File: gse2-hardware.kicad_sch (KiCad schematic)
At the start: 83 parts, among them J1 PJ-002A, J2 PJ-002A, J3 ARM Cortex Debug, J4 USB-C, J47 DSUB_15pin/VGA Veritical Fema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, J6 ARM, J7 0430451812, Q1 DMG3402L, U1 STM32F105RCT6, U2 AS78L05RTR-E1, U3 USBLC6-2SC6, U5 MP2338GTL-Z, U6 UA78M10CKVURG3, U7 BA78M20FP-E2, U8 MAX11614, Y1 16MHz

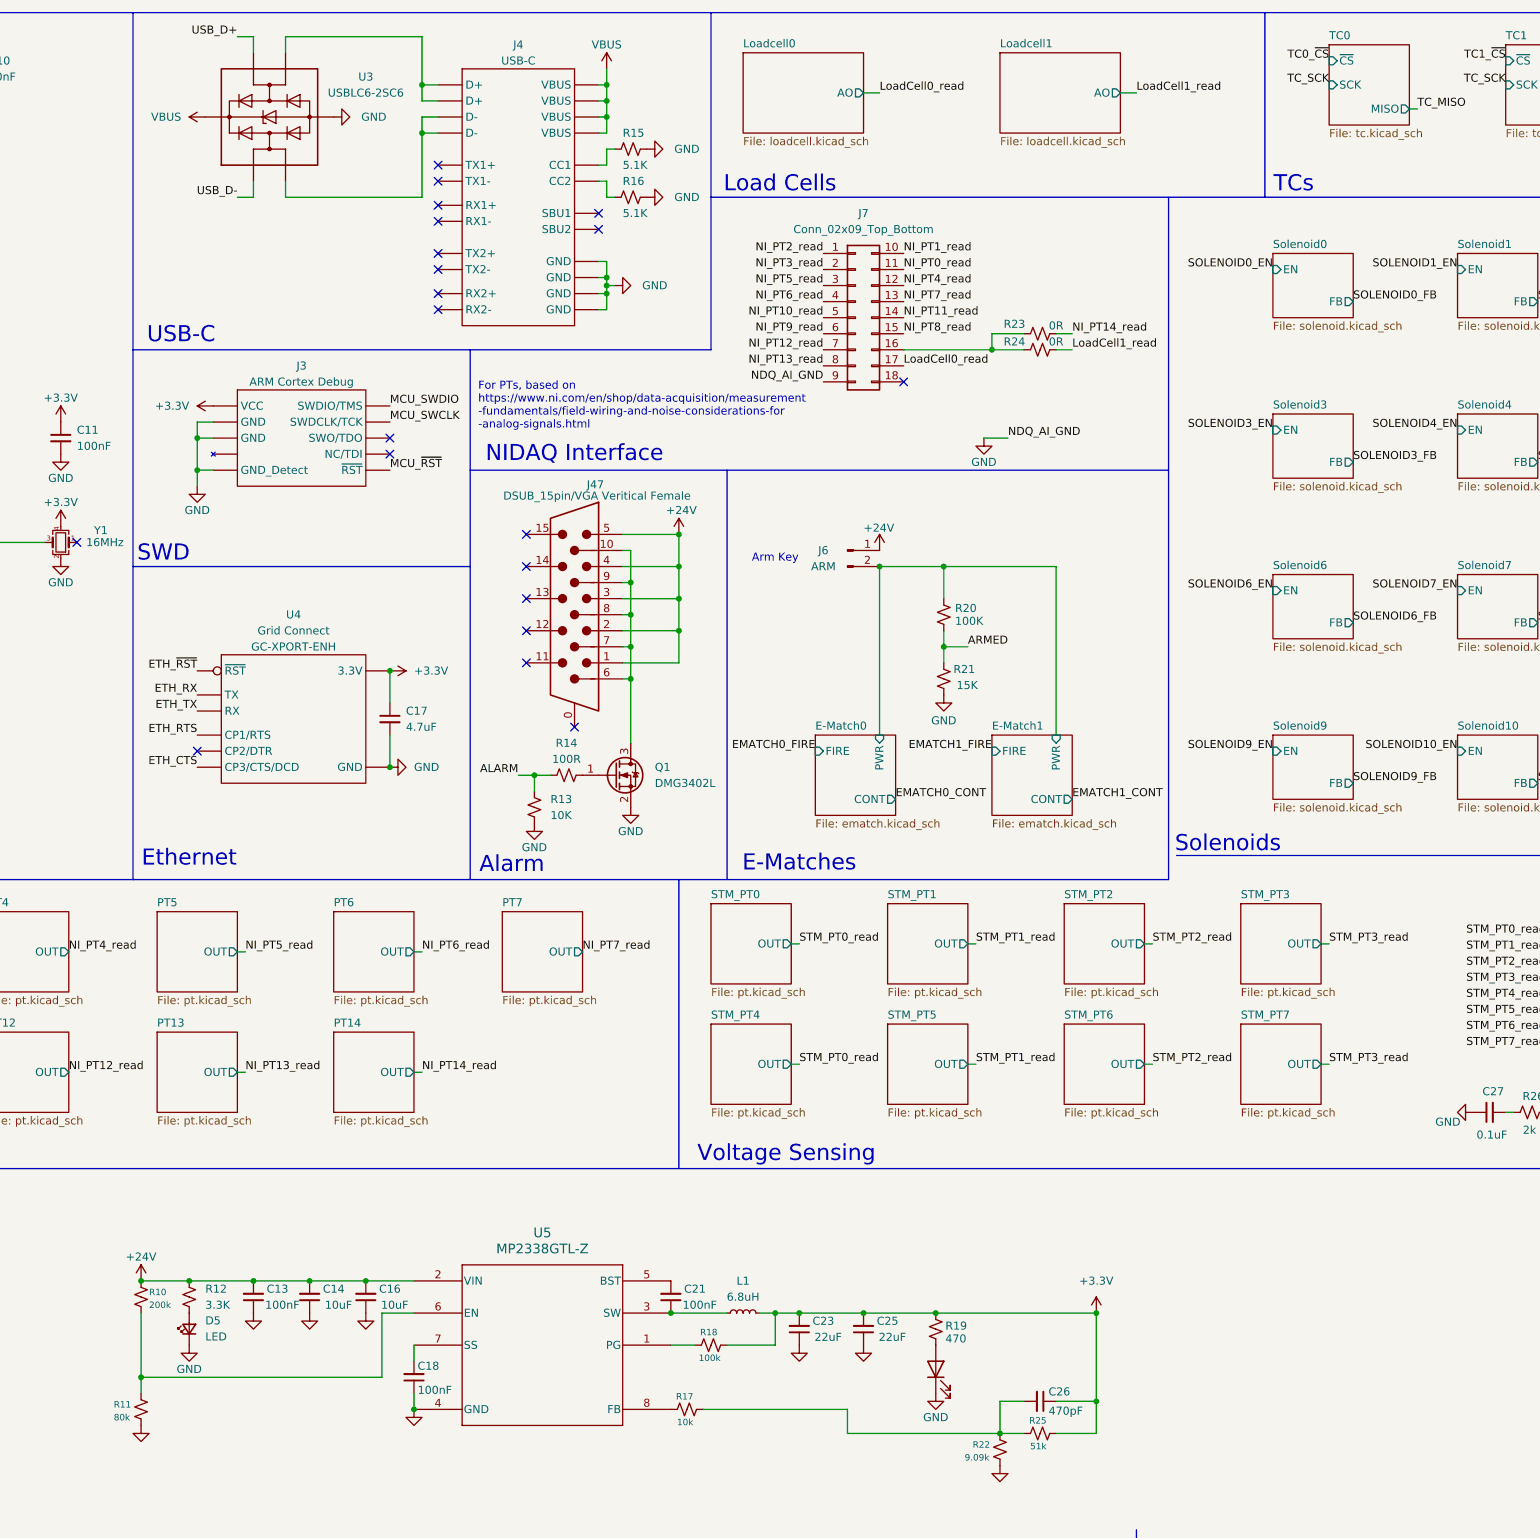
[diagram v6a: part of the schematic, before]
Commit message: GSE v2.1: Routing 90% done
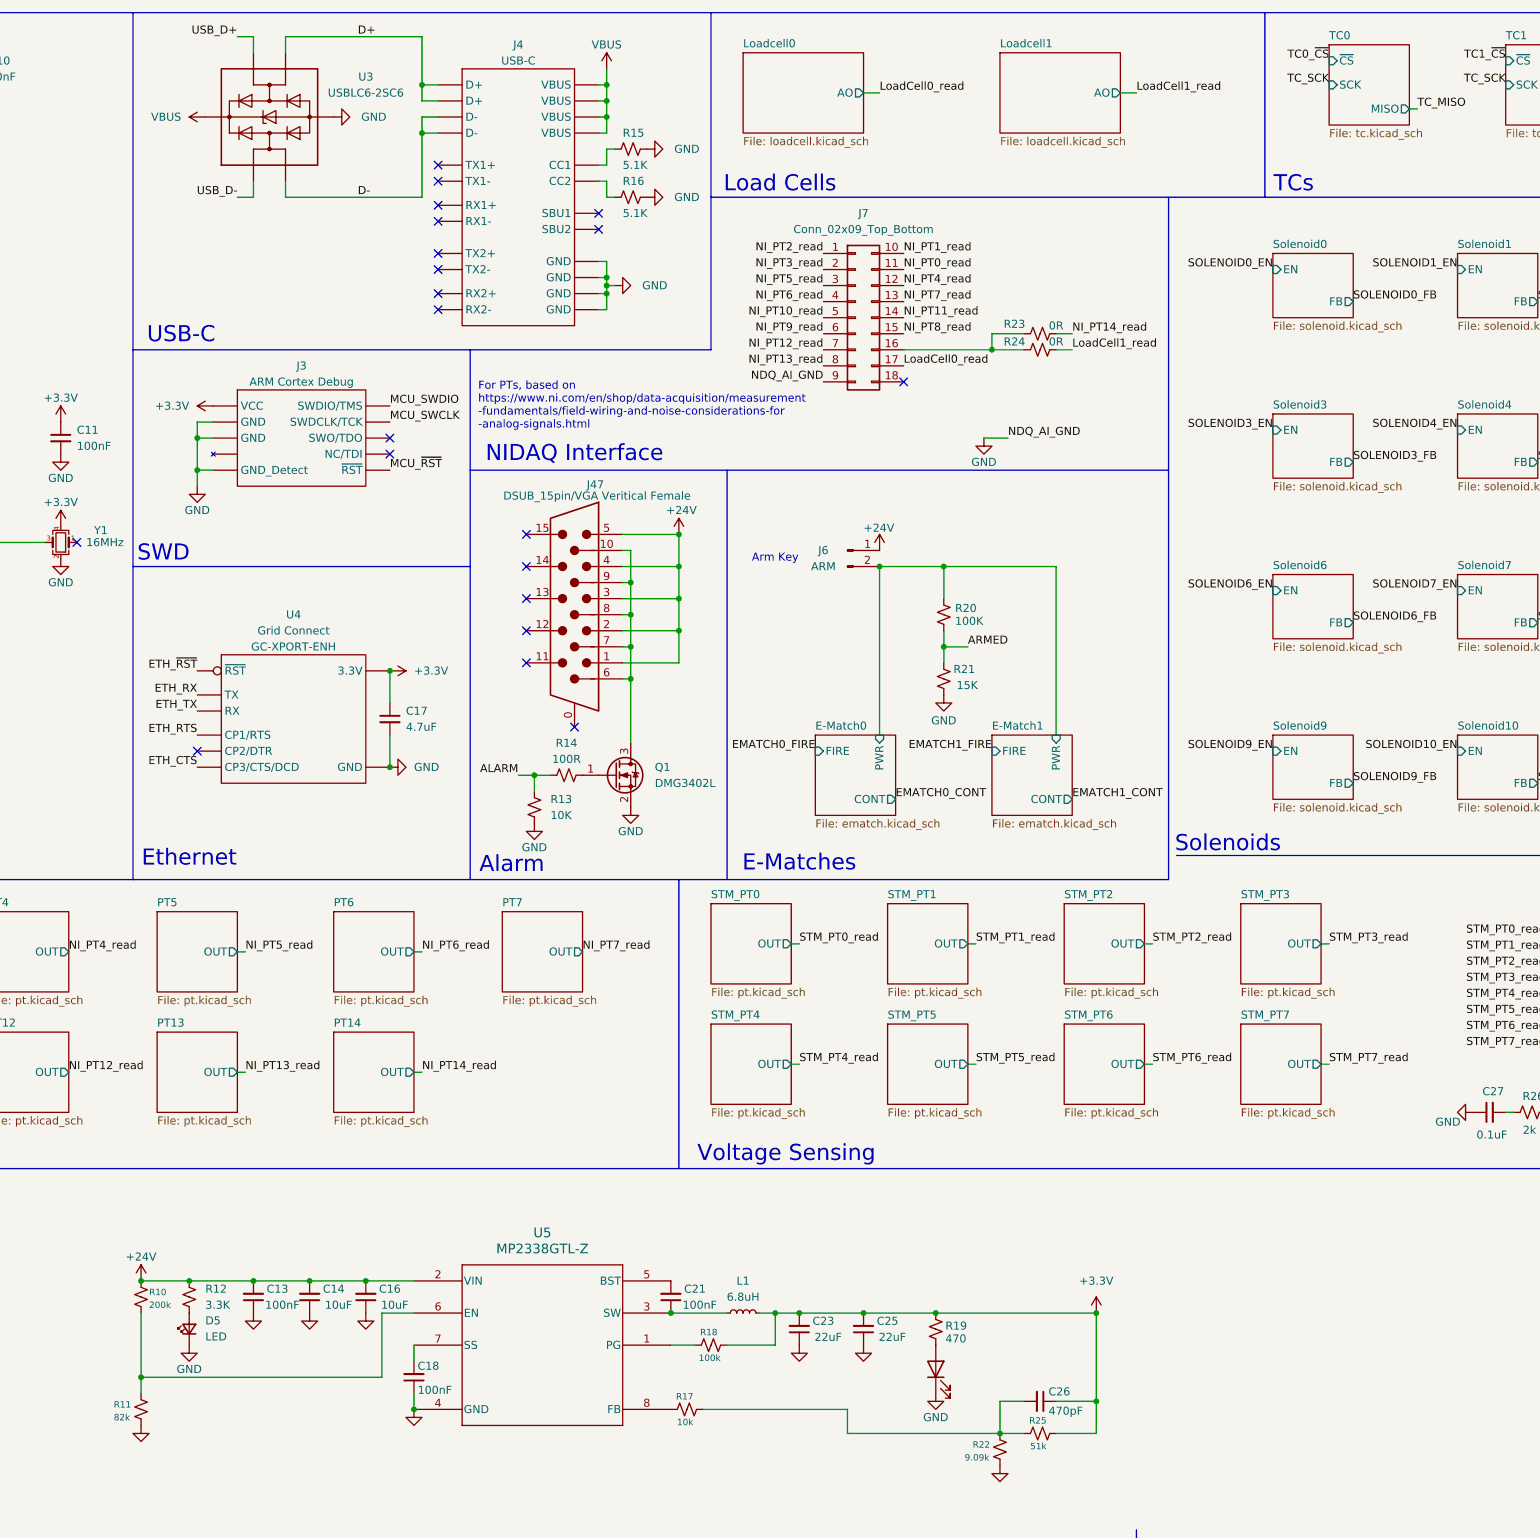
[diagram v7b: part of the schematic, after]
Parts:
- R11: value 80k -> 82k
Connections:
- net D-: now reaches J4.A7 (D-), J4.B7 (D-), U3.1 (I/O1)
- net D+: now reaches J4.A6 (D+), J4.B6 (D+), U3.3 (I/O2)
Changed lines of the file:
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@@
 		)
 	)
-	(label "STM_PT2_read"
-		(at 302.26 179.07 0)
-		(effects
-			(font
-				(size 1.27 1.27)
-			)
-			(justify left bottom)
-		)
-	)
 	(label "TC_SCK"
 		(at 55.88 121.92 180)
@@
 		)
 	)
+	(label "STM_PT5_read"
+		(at 274.32 179.07 0)
+		(effects
+			(font
+				(size 1.27 1.27)
+			)
+			(justify left bottom)
+		)
+	)
 	(label "NI_PT9_read"
 		(at 52.07 180.34 0)
@@
 		)
 	)
+	(label "D+"
+		(at 176.53 16.51 0)
+		(effects
+			(font
+				(size 1.27 1.27)
+			)
+			(justify left bottom)
+		)
+	)
 	(label "USB_D+"
 		(at 55.88 85.09 180)
@@
 		)
 	)
-	(label "STM_PT3_read"
-		(at 330.2 179.07 0)
-		(effects
-			(font
-				(size 1.27 1.27)
-			)
-			(justify left bottom)
-		)
-	)
 	(label "NI_PT3_read"
 		(at 104.14 161.29 0)
@@
 		)
 	)
-	(label "STM_PT1_read"
-		(at 274.32 179.07 0)
-		(effects
-			(font
-				(size 1.27 1.27)
-			)
-			(justify left bottom)
-		)
-	)
 	(label "TC2_~{CS}"
 		(at 55.88 92.71 180)
@@
 		)
 	)
+	(label "STM_PT7_read"
+		(at 330.2 179.07 0)
+		(effects
+			(font
+				(size 1.27 1.27)
+			)
+			(justify left bottom)
+		)
+	)
 	(label "SOLENOID5_EN"
 		(at 101.6 67.31 0)
@@
 		)
 	)
+	(label "D-"
+		(at 176.53 41.91 0)
+		(effects
+			(font
+				(size 1.27 1.27)
+			)
+			(justify left bottom)
+		)
+	)
 	(label "ARMED"
 		(at 101.6 92.71 0)
@@
 		)
 	)
-	(label "STM_PT0_read"
-		(at 246.38 179.07 0)
-		(effects
-			(font
-				(size 1.27 1.27)
-			)
-			(justify left bottom)
-		)
-	)
 	(label "PWR1"
 		(at 101.6 57.15 0)
@@
 		)
 	)
+	(label "STM_PT6_read"
+		(at 302.26 179.07 0)
+		(effects
+			(font
+				(size 1.27 1.27)
+			)
+			(justify left bottom)
+		)
+	)
 	(label "ETH_CTS"
 		(at 151.13 132.08 180)
@@
 		)
 	)
+	(label "STM_PT4_read"
+		(at 246.38 179.07 0)
+		(effects
+			(font
+				(size 1.27 1.27)
+			)
+			(justify left bottom)
+		)
+	)
 	(label "SOLENOID9_EN"
 		(at 55.88 127 180)
@@
 			)
 		)
-		(property "Value" "80k"
+		(property "Value" "82k"
 			(at 137.922 234.95 0)
 			(effects

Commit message: GSE v2.1 done, just waiting on prop rn to finalize their sensor list
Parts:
- removed U1: STM32F105RCT6, Package_QFP:LQFP-64_10x10mm_P0.5mm, symbol UCIRP-KiCAD-Lib:STM32F105RCT6
- removed U2: AS78L05RTR-E1, Package_TO_SOT_SMD:SOT-89-3, symbol UCIRP-KiCAD-Lib:Generic_Regulator_InputGroundOutput
- removed U4: ~, 0UCIRP-KiCAD-Lib:GC-XPORT, symbol UCIRP-KiCAD-Lib:GC-XPORT
- removed U5: MP2338GTL-Z, SOT583_MP2338_MNP, symbol UCIRP-KiCAD-Lib:MP2338GTL-Z
- removed U6: UA78M10CKVURG3, Package_TO_SOT_SMD:TO-252-2, symbol UCIRP-KiCAD-Lib:Generic_Regulator_InputGroundOutput
- removed U7: BA78M20FP-E2, Package_TO_SOT_SMD:TO-252-2, symbol UCIRP-KiCAD-Lib:Generic_Regulator_InputGroundOutput
- added D54, D55, D56: LED, LED_SMD:LED_0603_1608Metric, symbol Device:LED_Small
- added R267: 3.3K, Resistor_SMD:R_0603_1608Metric, symbol Device:R_Small_US
- added R268: 1k, Resistor_SMD:R_0603_1608Metric, symbol Device:R_Small_US
- added R269: 500R, Resistor_SMD:R_0603_1608Metric, symbol Device:R_Small_US
- added U1: STM32F105RCT6, 0UCIRP-KiCAD-Lib:MCU STM32F105RCT6, symbol 0UCIRP-KiCAD-Lib:MCU STM32F105RCT6
- added U2: AS78L05RTR-E1, 0UCIRP-KiCAD-Lib:5V_LDO AS78L05RTR-E1, symbol 0UCIRP-KiCAD-Lib:5V_LDO{colon} AS78L05RTR-E1
- added U4: GC-XPORT, 0UCIRP-KiCAD-Lib:Embedded_Ethernet GC-XPORT, symbol 0UCIRP-KiCAD-Lib:Embedded_Ethernet GC-XPORT
- added U5: 3V3_Buck MP2338GTL-Z, SOT583_MP2338_MNP, symbol 0UCIRP-KiCAD-Lib:3V3_Buck MP2338GTL-Z
- added U6: UA78M10CKVURG3, 0UCIRP-KiCAD-Lib:10V_LDO UA78M10CKVURG3, symbol 0UCIRP-KiCAD-Lib:10V_LDO UA78M10CKVURG3
- added U7: BA78M20FP-E2, 0UCIRP-KiCAD-Lib:20V_LDO BA78M20FP-E2, symbol 0UCIRP-KiCAD-Lib:20V_LDO_BA78M20FP-E2
- D3, D4: footprint Diode_SMD:D_PowerDI-5 -> 0UCIRP-KiCAD-Lib:Diode_Schottky (100V_80A) FSV8100V; Manufacturer Diodes -> (none); Part # SDT8A100P5-7 -> FSV8100V
- J1, J2: footprint 0UCIRP-KiCAD-Lib:CUI_PJ-002A -> Connector_BarrelJack:BarrelJack_GCT_DCJ200-10-A_Horizontal
- renumbered J47 to J5
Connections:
- net +10V: now also R268.2, U6.3 (VOUT)
- net +20V: now also R267.2, U7.3 (VOUT)
- net +24V: now also U2.3 (VIN), U5.2 (VIN), U6.1 (VIN), U7.1 (VIN)
- net +3.3V: now also U1.1 (VBAT), U1.13 (VDDA), U1.19 (VDD), U1.32 (VDD), U1.48 (VDD), U1.64 (VDD), U4.2 (3.3V)
- net +5V: now also R269.2, U2.1 (VOUT)
- net ALARM: now also U1.33 (PB12)
- net ARMED: now also U1.36 (PB15)
- net EMATCH0_CONT: now also U1.38 (PC7)
- net EMATCH0_FIRE: now also U1.37 (PC6)
- net EMATCH1_CONT: now also U1.40 (PC9)
- net EMATCH1_FIRE: now also U1.39 (PC8)
- net ETH_CTS: now also U1.35 (PB14), U4.8 (CP3/CTS/DCD)
- net ETH_RTS: now also U1.34 (PB13), U4.6 (CP1/RTS)
- net ETH_RX: now also U1.30 (PB11), U4.4 (TX)
- net ETH_TX: now also U1.29 (PB10), U4.5 (RX)
- net ETH_~{RST}: now also U1.28 (PB2), U4.3 (~{RST})
- net EXT_ADC_SCL: now also U1.58 (PB6)
- net EXT_ADC_SDA: now also U1.59 (PB7)
- net GND: now also D54.1 (K), D55.1 (K), D56.1 (K), U1.12 (VSSA), U1.18 (VSS), U1.31 (VSS), U1.47 (VSS), U1.60 (BOOT0), U1.63 (VSS), U2.2 (GND), U4.1 (GND), U5.4 (GND), U6.2 (GND), U7.2 (GND)
- net MCU_SWCLK: now also U1.49 (PA14)
- net MCU_SWDIO: now also U1.46 (PA13)
- net MCU_~{RST}: now also U1.7 (~{RST})
- net PWR0: now also U1.26 (PB0)
- net PWR1: now also U1.27 (PB1)
- net SOLENOID0_EN: now also U1.4 (PC15)
- net SOLENOID0_FB: now also U1.8 (PC0)
- net SOLENOID10_EN: now also U1.24 (PC4)
- net SOLENOID10_FB: now also U1.22 (PA6)
- net SOLENOID11_EN: now also U1.25 (PC5)
- net SOLENOID11_FB: now also U1.23 (PA7)
- net SOLENOID1_EN: now also U1.3 (PC14)
- net SOLENOID1_FB: now also U1.9 (PC1)
- net SOLENOID2_EN: now also U1.2 (PC13)
- net SOLENOID2_FB: now also U1.10 (PC2)
- net SOLENOID3_EN: now also U1.62 (PB9)
- net SOLENOID3_FB: now also U1.11 (PC3)
- net SOLENOID4_EN: now also U1.61 (PB8)
- net SOLENOID4_FB: now also U1.14 (PA0)
- net SOLENOID5_EN: now also U1.57 (PB5)
- net SOLENOID5_FB: now also U1.15 (PA1)
- net SOLENOID6_EN: now also U1.56 (PB4)
- net SOLENOID6_FB: now also U1.16 (PA2)
- net SOLENOID7_EN: now also U1.55 (PB3)
- net SOLENOID7_FB: now also U1.17 (PA3)
- net SOLENOID8_EN: now also U1.54 (PD2)
- net SOLENOID8_FB: now also U1.20 (PA4)
- net SOLENOID9_EN: now also U1.53 (PC12)
- net SOLENOID9_FB: now also U1.21 (PA5)
- net TC0_~{CS}: now also U1.41 (PA8)
- net TC1_~{CS}: now also U1.43 (PA10)
- net TC2_~{CS}: now also U1.50 (PA15)
- net TC_MISO: now also U1.52 (PC11)
- net TC_SCK: now also U1.51 (PC10)
- net USB_D+: now also U1.45 (PA12)
- net USB_D-: now also U1.44 (PA11)
- net at R17.1: now also U5.8 (FB)
- net at R2.1, R3.2: now also U1.42 (PA9)
- net at Y1.3: now also U1.5 (PD0)
- net at C18.2: now also U5.7 (SS)
- net at R10.2, R11.1: now also U5.6 (EN)
- net at R18.1: now also U5.1 (PG)
- net at C21.1, L1.1: now also U5.3 (SW)
- net at C21.2: now also U5.5 (BST)
- new net: D55.2 (A), R268.1
- new net: D54.2 (A), R267.1
- new net: D56.2 (A), R269.1
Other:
- note added: "Switch to BA7820FP-E2 for 1A output in future maybe"
- moved on the sheet: C19, C20, C22, C24
